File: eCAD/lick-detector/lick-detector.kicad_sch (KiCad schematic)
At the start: 5 parts, among them J1 J_PinHeader_01x03_2.54_V

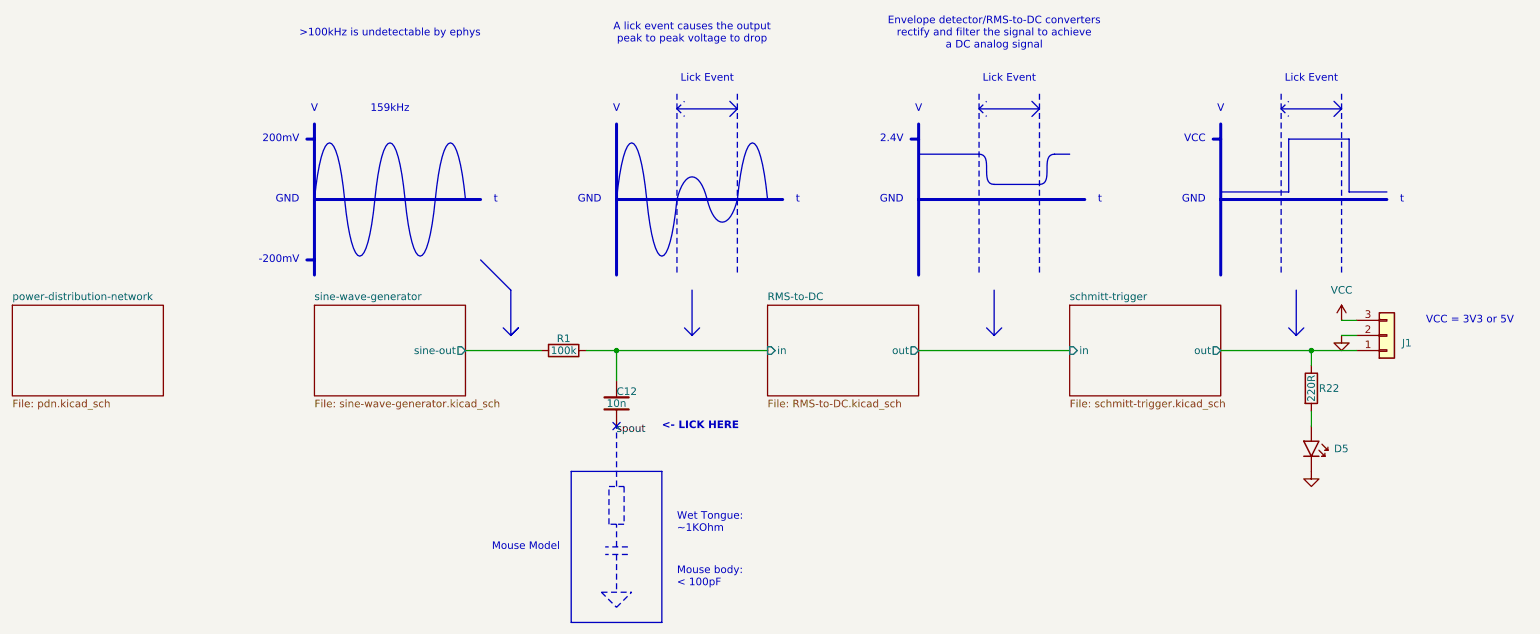
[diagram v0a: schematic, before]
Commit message: Number of upgrades complete: - Lower amplitude sine wave generator - Improved debug connector layout - Brightness of LED decreased - README updated with guide and areas for documentation - .gitignore added to ignore backup files and temporary files
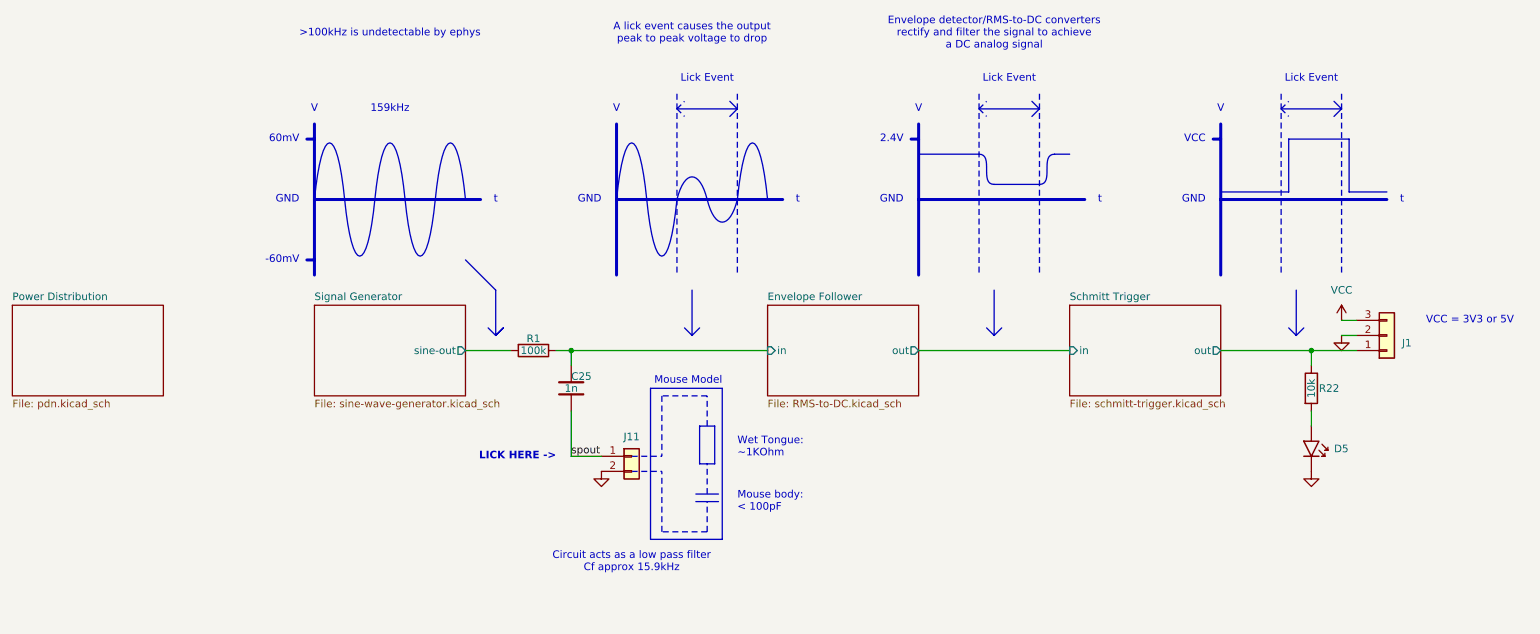
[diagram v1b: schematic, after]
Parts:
- removed C12: 10n, !fablabs-kicad-library:C_0603_1608M, symbol !fablabs-kicad-library:C_0603_10n_50V_X7R
- removed R22: 220R, !fablabs-kicad-library:R_0603_1608M, symbol !fablabs-kicad-library:R_0603_220R
- added C25: 1n, !fablabs-kicad-library:C_0603_1608M, symbol !fablabs-kicad-library:C_0603_1n_50V_X7R
- added J11: J_PinHeader_01x02_2.54_V, !fablabs-kicad-library:J_PinHeader_01x02_2.54_V, symbol !fablabs-kicad-library:J_PinHeader_01x02_2.54_V
- added R22: 10k, !fablabs-kicad-library:R_0603_1608M, symbol !fablabs-kicad-library:R_0603_10k
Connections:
- net GND: now also J11.2 (Pin_2)
- net Envelope Follower/in: now also C25.2
- net Schmitt Trigger/out: now also R22.2
- net spout: now also C25.1, J11.1 (Pin_1)
- net at D5.2 (A): now also R22.1
- no-connect marks 1 -> 0
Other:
- sheet RMS-to-DC renamed Envelope Follower
- sheet power-distribution-network renamed Power Distribution
- sheet schmitt-trigger renamed Schmitt Trigger
- sheet sine-wave-generator renamed Signal Generator
- note added: "-60mV"
- note added: "60mV"
- note added: "Circuit acts as a low pass filter Cf approx 15.9kHz"
- note added: "LICK HERE ->"
- note removed: "-200mV"
- note removed: "200mV"
- note removed: "<- LICK HERE"
- moved on the sheet: R1
